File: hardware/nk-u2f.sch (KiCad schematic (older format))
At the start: 23 parts, among them J1 USB_Plug, P1 TouchPAD, U1 EFM8UB1xFxxG-QFN20, U2 MTCH101, U3 DF5A5.6JE, U4 ATECC508A

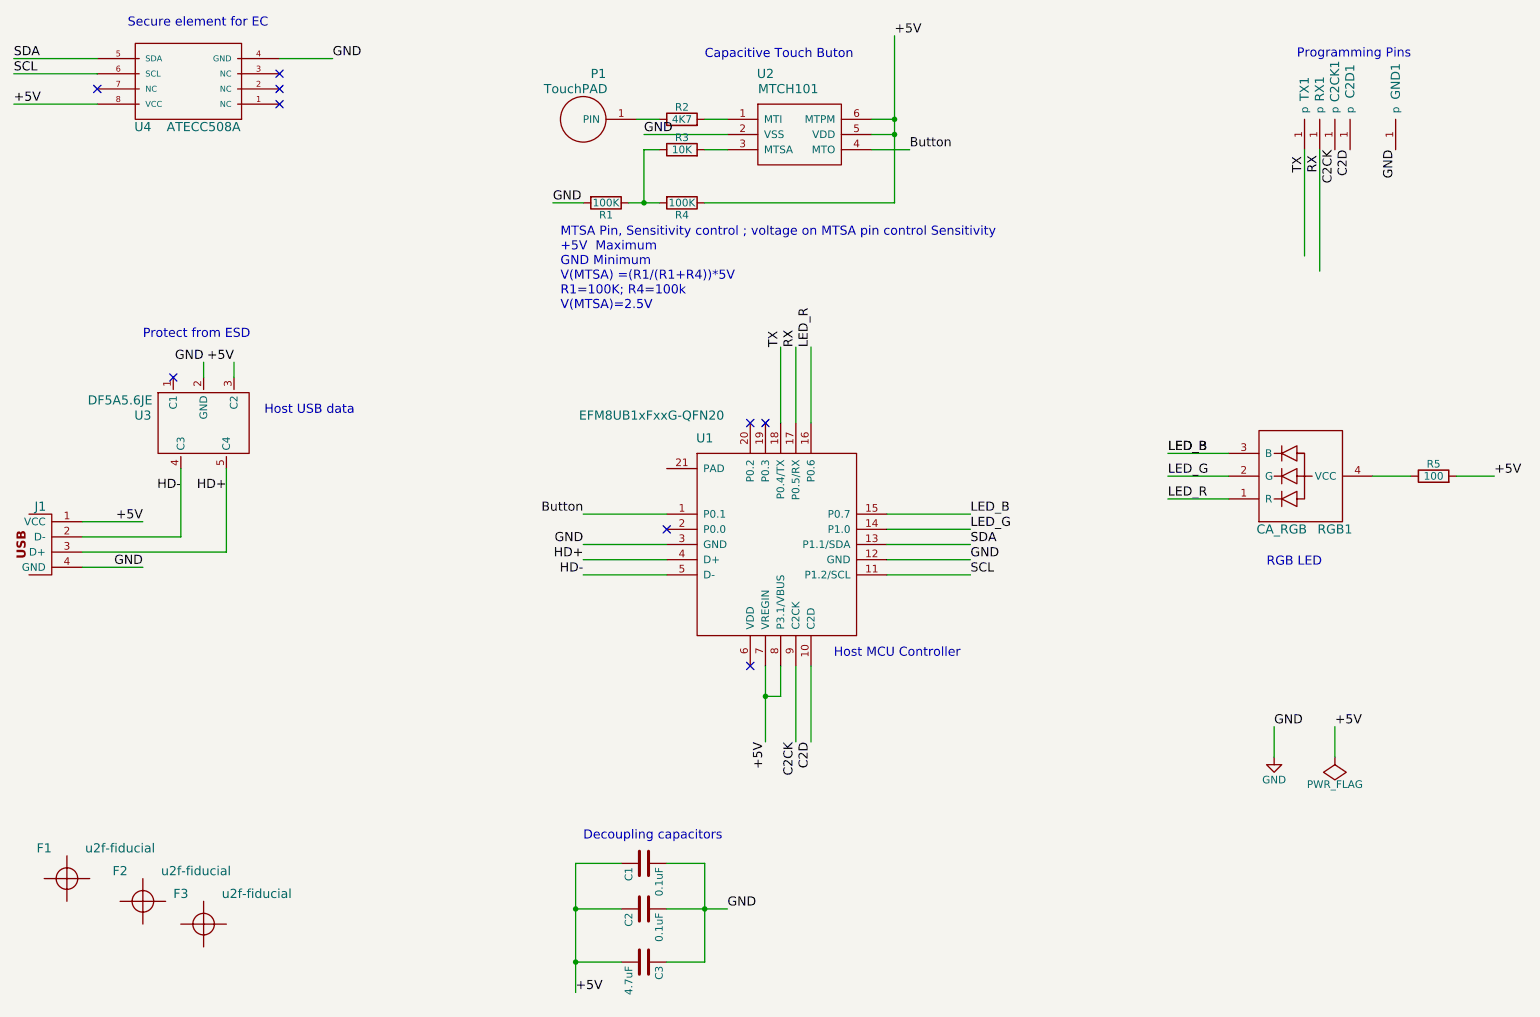
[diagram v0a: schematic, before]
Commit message: PCB layout Updated
All resistors capacitors and LED are 0402 packages.
Programming headeder updated.
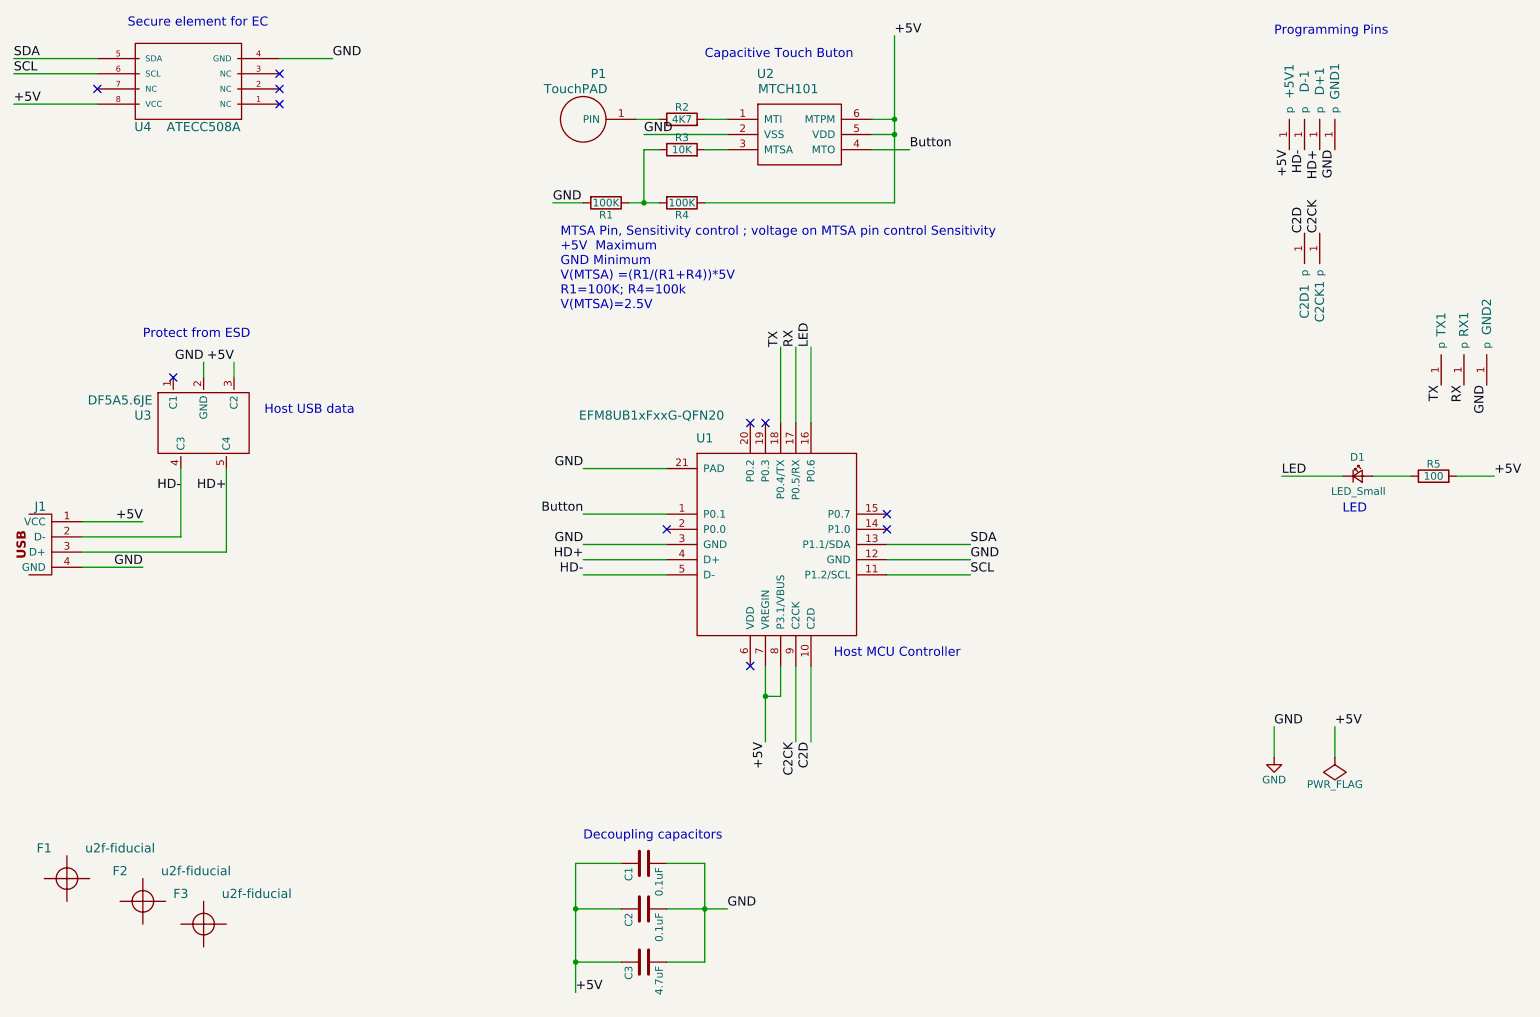
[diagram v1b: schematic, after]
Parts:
- removed RGB1: CA_RGB, footprints:LED-0606, symbol CA_RGB-RESCUE-u2f-zero
- added +5V1, D+1, D-1, GND2: debug-pin, footprints:Prog_Pad, symbol debug-pin
- added D1: LED_Small, LEDs:LED_0402, symbol LED_Small
- C1, C2: Distributer Link http://www.digikey.com/product-detail/en/CL05A104MP5NNNC/12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 -> ?; Distributer PN 1276-1443-1-ND -> ?; MFG Name Samsung Electro-Mechanics America, Inc -> ?; MFG Part Num CL05A104MP5NNNC -> ?
- C2CK1, C2D1, GND1, RX1, TX1: footprint footprints:debug -> footprints:Prog_Pad
- C3: footprint Capacitors_SMD:C_0603 -> Capacitors_SMD:C_0402; Distributer Link http://www.digikey.com/product-detail/en/CL10B475KQ8NQNC/12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 -> ?; Distributer PN 1276-2087-1-ND -> ?; MFG Name Samsung Electro-Mechanics America, Inc -> ?; MFG Part Num CL10B475KQ8NQNC -> ?
- R1, R2, R3, R4: footprint Resistors_SMD:R_0603 -> Resistors_SMD:R_0402
- R5: footprint Resistors_SMD:R_0603 -> Resistors_SMD:R_0402; Distributer Link http://www.digikey.com/product-detail/en/CRCW0603100RFKEA/5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 -> ?; Distributer PN 541-100HCT-ND -> ?; MFG Name Vishay Dale -> ?; MFG Part Num CRCW0603100RFKEA -> ?
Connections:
- net +5V: now also C3.1, +5V1.1 (p); no longer C3.2
- net GND: now also C3.2, U1.21 (PAD), GND2.1 (p); no longer C3.1
- net HD+: now also D+1.1 (p)
- net HD-: now also D-1.1 (p)
- net at R5.1: now also D1.2 (A)
- net LED_B: no longer names the net of U1.15 (P0.7)
- net LED_G: no longer names the net of U1.14 (P1.0)
- net LED_R renamed LED
- net LED: now also D1.1 (K)
- no-connect marks 9 -> 11
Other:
- note added: "LED\n"
- note removed: "RGB LED\n"
- moved on the sheet: C2CK1, C2D1, GND1, RX1, TX1

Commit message: Touch Pad senitivity updated
Touch Pad senitivity updated
Programming pads updated to compatible with protoboard pitch
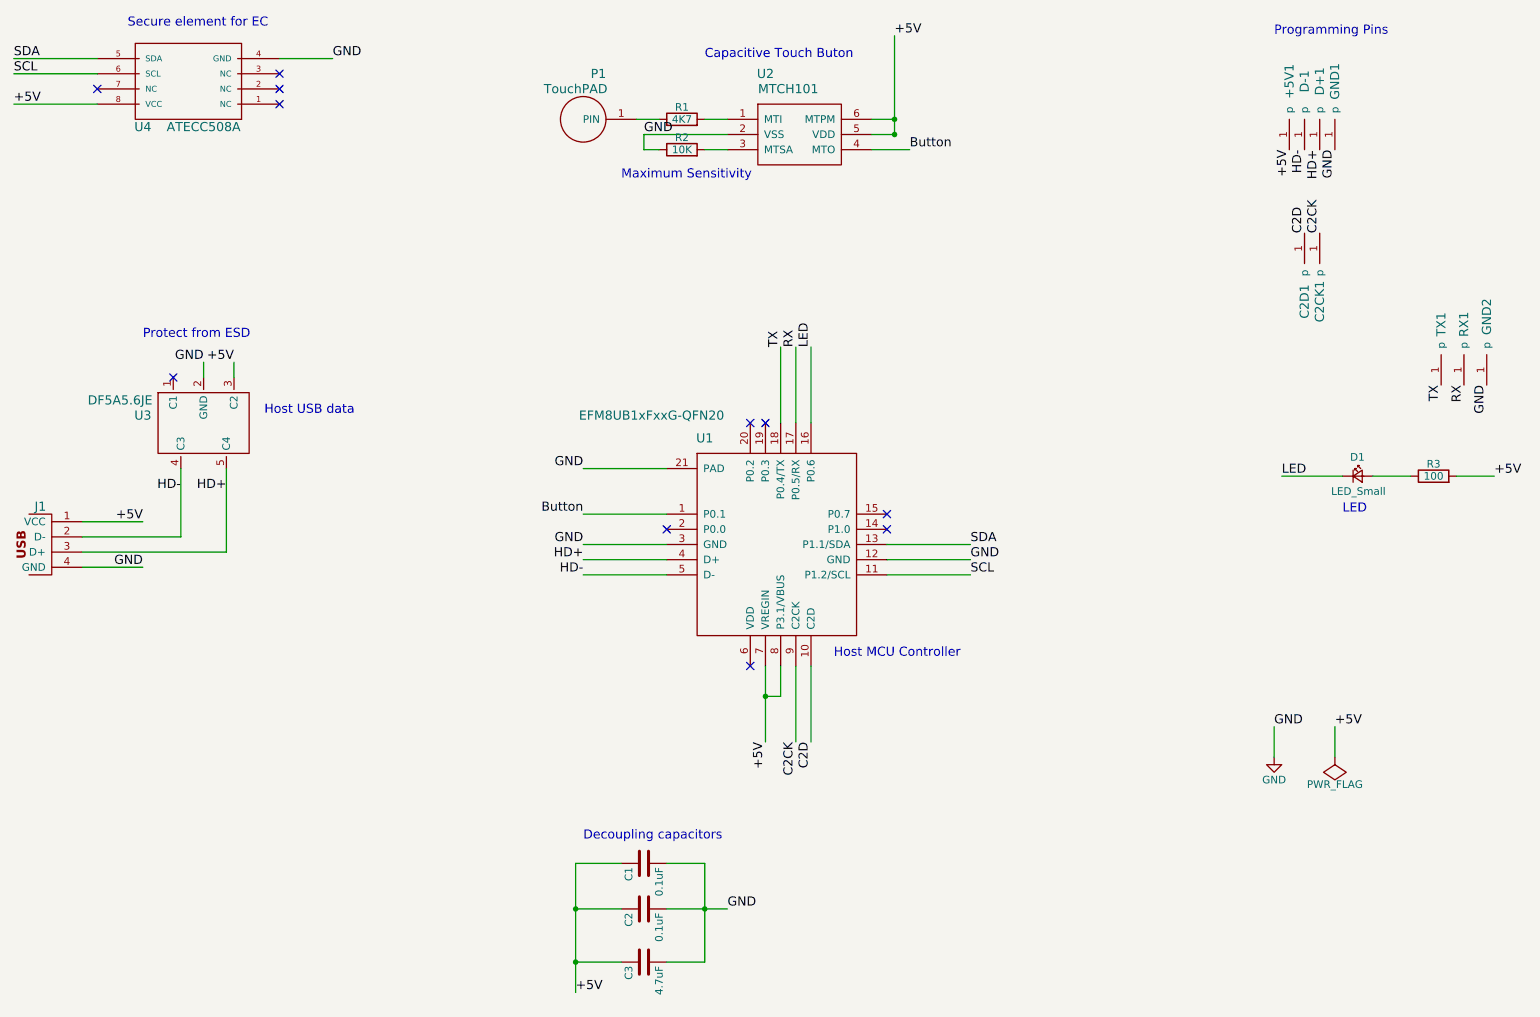
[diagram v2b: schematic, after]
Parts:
- removed F1, F2, F3: u2f-fiducial, footprints:u2f-fiducial, symbol u2f-fiducial
- removed R1, R4: 100K, Resistors_SMD:R_0402, symbol R
- renumbered R2 to R1, R3 to R2, R5 to R3
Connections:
- net GND: now also R2.1
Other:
- note added: "Maximum Sensitivity\n"
- note removed: "MTSA Pin, Sensitivity control ; voltage on MTSA pin control Sensitivity\n+5V Maximum\nGND Minimum\nV(MTSA) =(R1/(R1+R4))*5V\nR1=100K; R4=100k\nV(MTSA)=2.5V\n\n\n\n"
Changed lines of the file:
@@
 Sheet 1 1
 Title "Nitrokey FIDO U2F"
-Date "2017-03-07"
-Rev "R1"
+Date "2017-06-13"
+Rev "R2"
 Comp "MikroStarTech"
 Comment1 "Muhammad Atif Riaz"
@@
 HD+
 $Comp
-L R R5
+L R R3
 U 1 1 56857B9B
 P 10300 3950
-F 0 "R5" V 10380 3950 50  0000 C CNN
+F 0 "R3" V 10380 3950 50  0000 C CNN
 F 1 "100" V 10300 3950 50  0000 C CNN
 F 2 "Resistors_SMD:R_0402" V 10230 3950 50  0001 C CNN
@@
 GND
 $Comp
-L u2f-fiducial F1
-U 1 1 571C39BB
-P 1300 6600
-F 0 "F1" H 1150 6800 60  0000 C CNN
-F 1 "u2f-fiducial" H 1650 6800 60  0000 C CNN
-F 2 "footprints:u2f-fiducial" H 1300 6600 60  0001 C CNN
-F 3 "" H 1300 6600 60  0000 C CNN
-	1    1300 6600
-	1    0    0    -1
-$EndComp
-$Comp
-L u2f-fiducial F2
-U 1 1 571C3A1E
-P 1800 6750
-F 0 "F2" H 1650 6950 60  0000 C CNN
-F 1 "u2f-fiducial" H 2150 6950 60  0000 C CNN
-F 2 "footprints:u2f-fiducial" H 1800 6750 60  0001 C CNN
-F 3 "" H 1800 6750 60  0000 C CNN
-	1    1800 6750
-	1    0    0    -1
-$EndComp
-$Comp
-L u2f-fiducial F3
-U 1 1 571C3A85
-P 2200 6900
-F 0 "F3" H 2050 7100 60  0000 C CNN
-F 1 "u2f-fiducial" H 2550 7100 60  0000 C CNN
-F 2 "footprints:u2f-fiducial" H 2200 6900 60  0001 C CNN
-F 3 "" H 2200 6900 60  0000 C CNN
-	1    2200 6900
-	1    0    0    -1
-$EndComp
-$Comp
 L MTCH101 U2
 U 1 1 58B45395
@@
 $EndComp
 $Comp
-L R R2
+L R R1
 U 1 1 58B46D59
 P 5350 1600
-F 0 "R2" V 5430 1600 50  0000 C CNN
+F 0 "R1" V 5430 1600 50  0000 C CNN
 F 1 "4K7" V 5350 1600 50  0000 C CNN
 F 2 "Resistors_SMD:R_0402" V 5280 1600 50  0001 C CNN
@@
 Button
 $Comp
-L R R3
+L R R2
 U 1 1 58B4B268
 P 5350 1800
-F 0 "R3" V 5430 1800 50  0000 C CNN
+F 0 "R2" V 5430 1800 50  0000 C CNN
 F 1 "10K" V 5350 1800 50  0000 C CNN
 F 2 "Resistors_SMD:R_0402" V 5280 1800 50  0001 C CNN
@@
 	6750 1700 6600 1700
 Wire Wire Line
-	6750 1050 6750 2150
+	6750 1050 6750 1700
 Wire Wire Line
 	5500 1800 5650 1800
-$Comp
-L R R1
-U 1 1 58B4C1B5
-P 4850 2150
-F 0 "R1" V 4930 2150 50  0000 C CNN
-F 1 "100K" V 4850 2150 50  0000 C CNN
-F 2 "Resistors_SMD:R_0402" V 4780 2150 50  0001 C CNN
-F 3 "http://www.vishay.com/docs/20035/dcrcwe3.pdf" H 4850 2150 50  0001 C CNN
-F 4 "Vishay Dale" H 4850 2150 60  0001 C CNN "MFG Name"
-F 5 "?" H 4850 2150 60  0001 C CNN "MFG Part Num"
-F 6 "?" H 4850 2150 60  0001 C CNN "Distributer PN"
-F 7 "?" H 4850 2150 60  0001 C CNN "Distributer Link"
-	1    4850 2150
-	0    1    1    0
-$EndComp
-$Comp
-L R R4
-U 1 1 58B4C27F
-P 5350 2150
-F 0 "R4" V 5430 2150 50  0000 C CNN
-F 1 "100K" V 5350 2150 50  0000 C CNN
-F 2 "Resistors_SMD:R_0402" V 5280 2150 50  0001 C CNN
-F 3 "http://www.vishay.com/docs/20035/dcrcwe3.pdf" H 5350 2150 50  0001 C CNN
-F 4 "Vishay Dale" H 5350 2150 60  0001 C CNN "MFG Name"
-F 5 "?" H 5350 2150 60  0001 C CNN "MFG Part Num"
-F 6 "?" H 5350 2150 60  0001 C CNN "Distributer PN"
-F 7 "?" H 5350 2150 60  0001 C CNN "Distributer Link"
-	1    5350 2150
-	0    1    1    0
-$EndComp
-Wire Wire Line
-	6750 2150 5500 2150
 Connection ~ 6750 1700
 Wire Wire Line
-	5000 2150 5200 2150
-Wire Wire Line
 	5200 1800 5100 1800
-Wire Wire Line
-	5100 1800 5100 2150
-Connection ~ 5100 2150
-Wire Wire Line
-	4700 2150 4500 2150
-Text Label 4500 2150 0    60   ~ 0
-GND
 Text Label 6750 1050 0    60   ~ 0
 +5V
@@
 Text Notes 5500 1400 0    60   ~ 0
 Capacitive Touch Buton\n\n\n
-Text Notes 4550 3150 0    60   ~ 0
-MTSA Pin, Sensitivity control ; voltage on MTSA pin control Sensitivity\n+5V  Maximum\nGND Minimum\nV(MTSA) =(R1/(R1+R4))*5V\nR1=100K; R4=100k\nV(MTSA)=2.5V\n\n\n\n
+Text Notes 4950 2000 0    60   ~ 0
+Maximum Sensitivity\n
 $Comp
 L LED_Small D1
@@
 Text Label 10650 3350 3    60   ~ 0
 GND
+Wire Wire Line
+	5100 1800 5100 1700
 $EndSCHEMATC
